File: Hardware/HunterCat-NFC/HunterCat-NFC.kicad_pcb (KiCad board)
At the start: 2 copper layers, 80.7 x 33.5 mm, 71 parts, among them J1 Battery, J2 Conn_01x06_Female, P1 USB_C_Plug_USB2.0, Q1 DMG3415U-7, SW1 RESET, SW2 GPIO, SW3 GPIO1, SW4 GPIO2, SW5 ON, U1 ATSAMD21E18A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

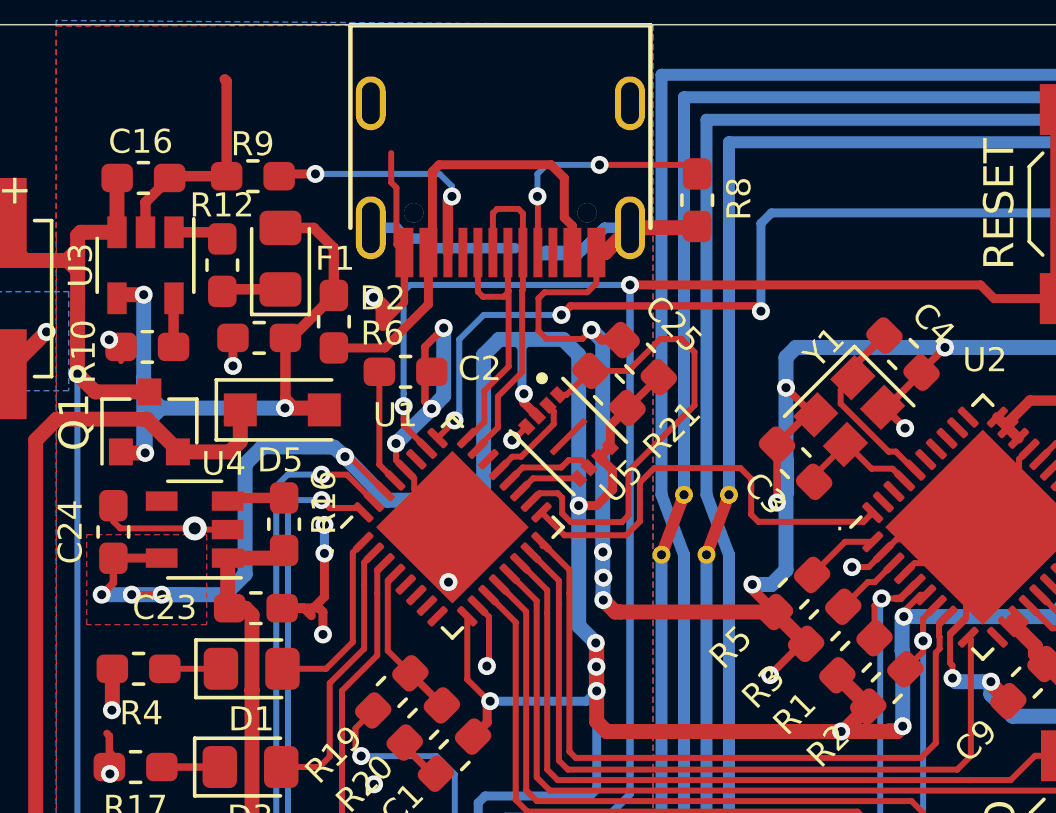
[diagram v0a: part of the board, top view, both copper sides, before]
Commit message: changed flash footprint dimensions
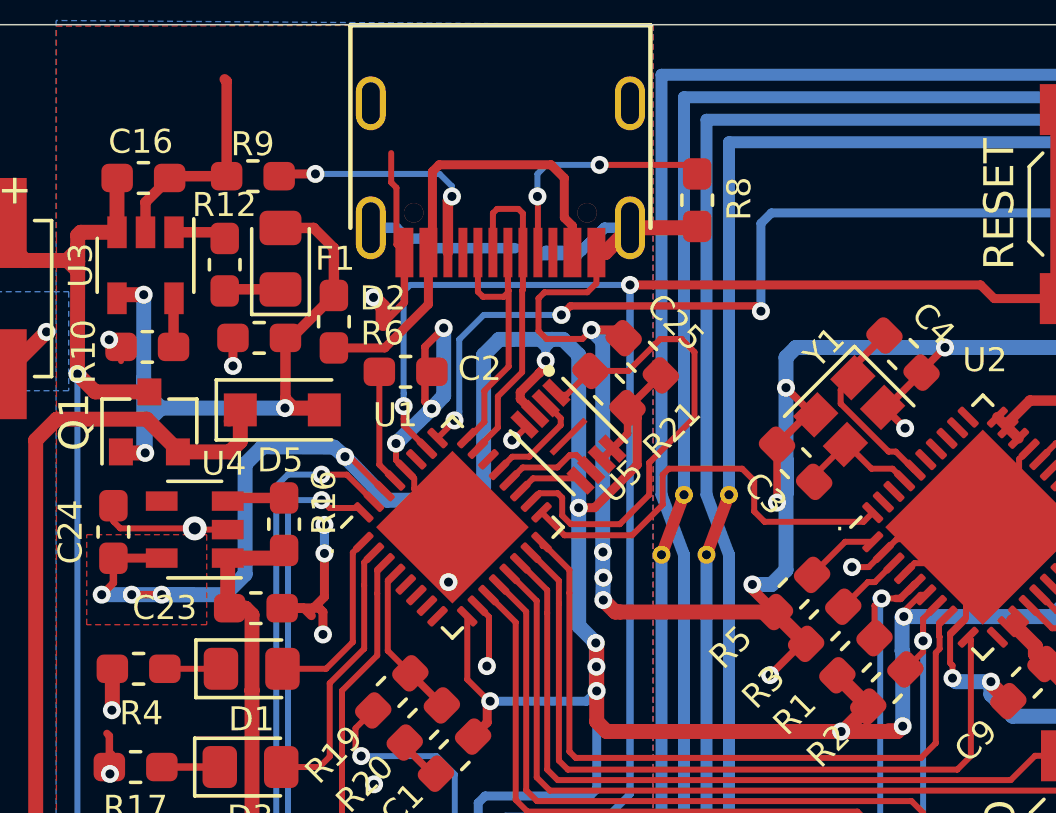
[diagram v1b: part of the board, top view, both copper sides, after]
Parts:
- moved C25 0.09 mm to (122.5, 86.6)
- moved R12 0.08 mm to (108.6, 83.5)
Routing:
- net +3V3: track 134.0 -> 135.7 mm
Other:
- net class Default removed
